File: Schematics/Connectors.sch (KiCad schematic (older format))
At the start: 106 parts, among them P601 CONN_02X05, P602 CONN_02X05, P603 CONN_02X05, P604 CONN_02X05, P605 CONN_02X05, P606 CONN_6X2, P607 CONN_02X05, P608 CONN_02X05, P609 CONN_02X20, P610 CONN_02X05, P611 CONN_02X05, P612 CONN_02X05, P613 CONN_02X05, P614 CONN_02X05, P615 CONN_02X05, P616 CONN_02X05

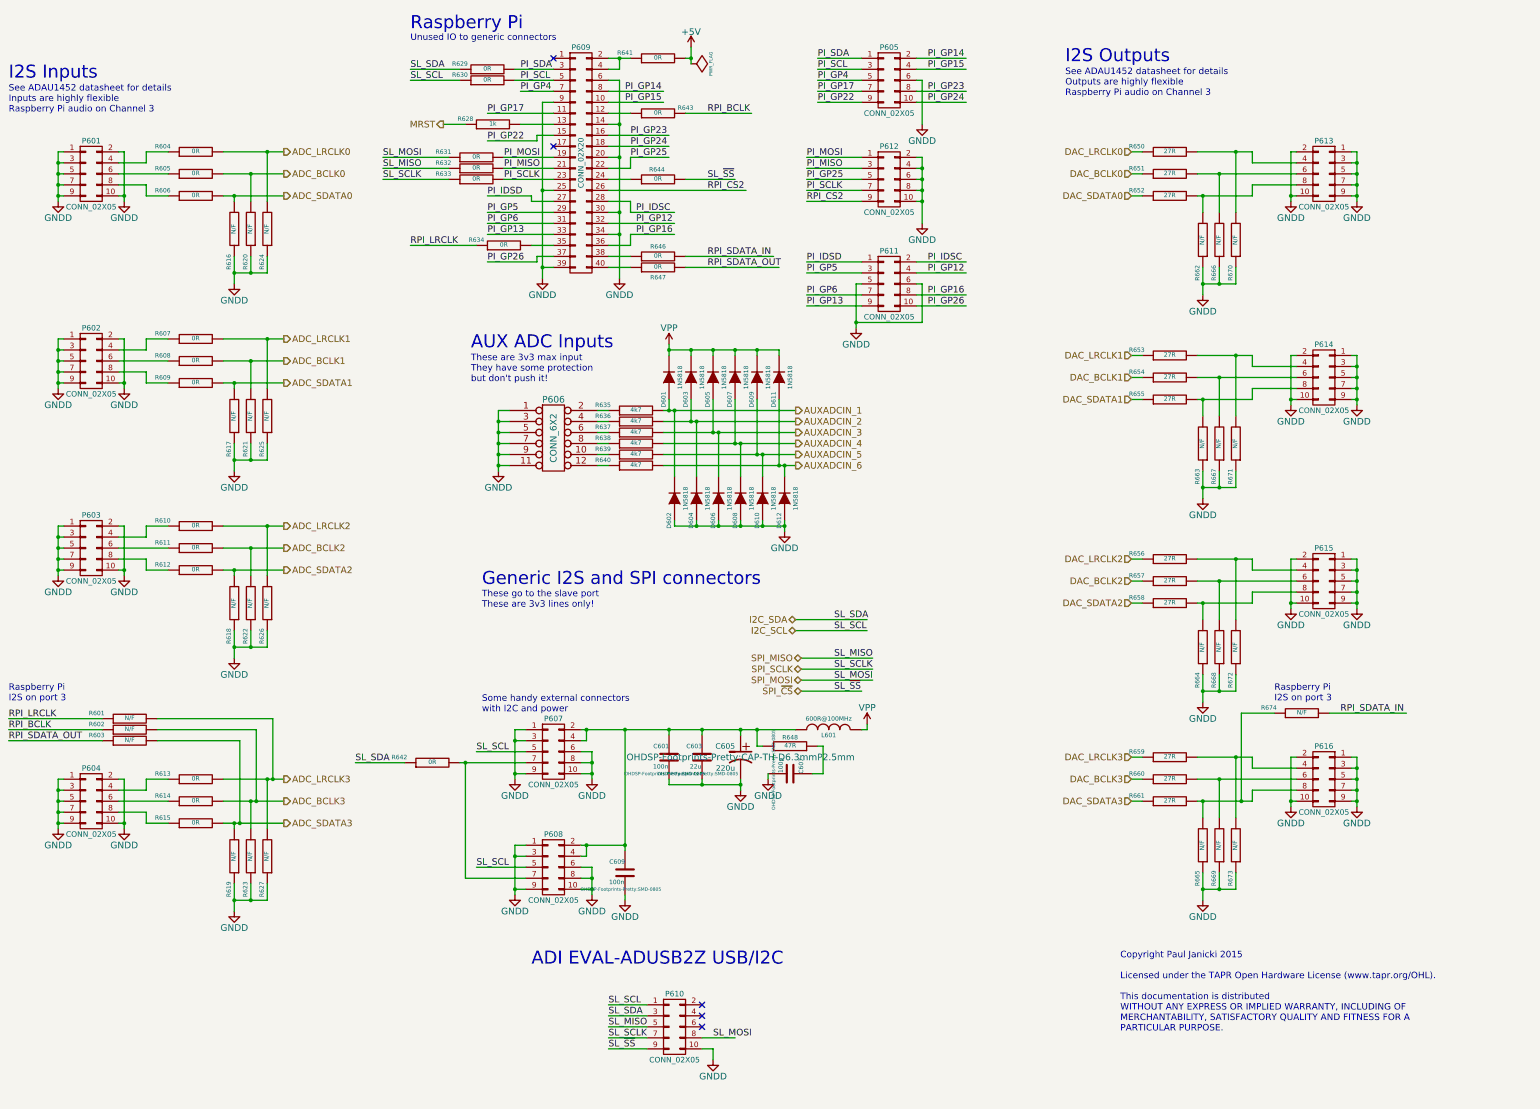
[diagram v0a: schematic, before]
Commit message: WIP
Removed Slave SPI as only really need I2C
Should free up some space on the board.
May look to change U.fl to SMA
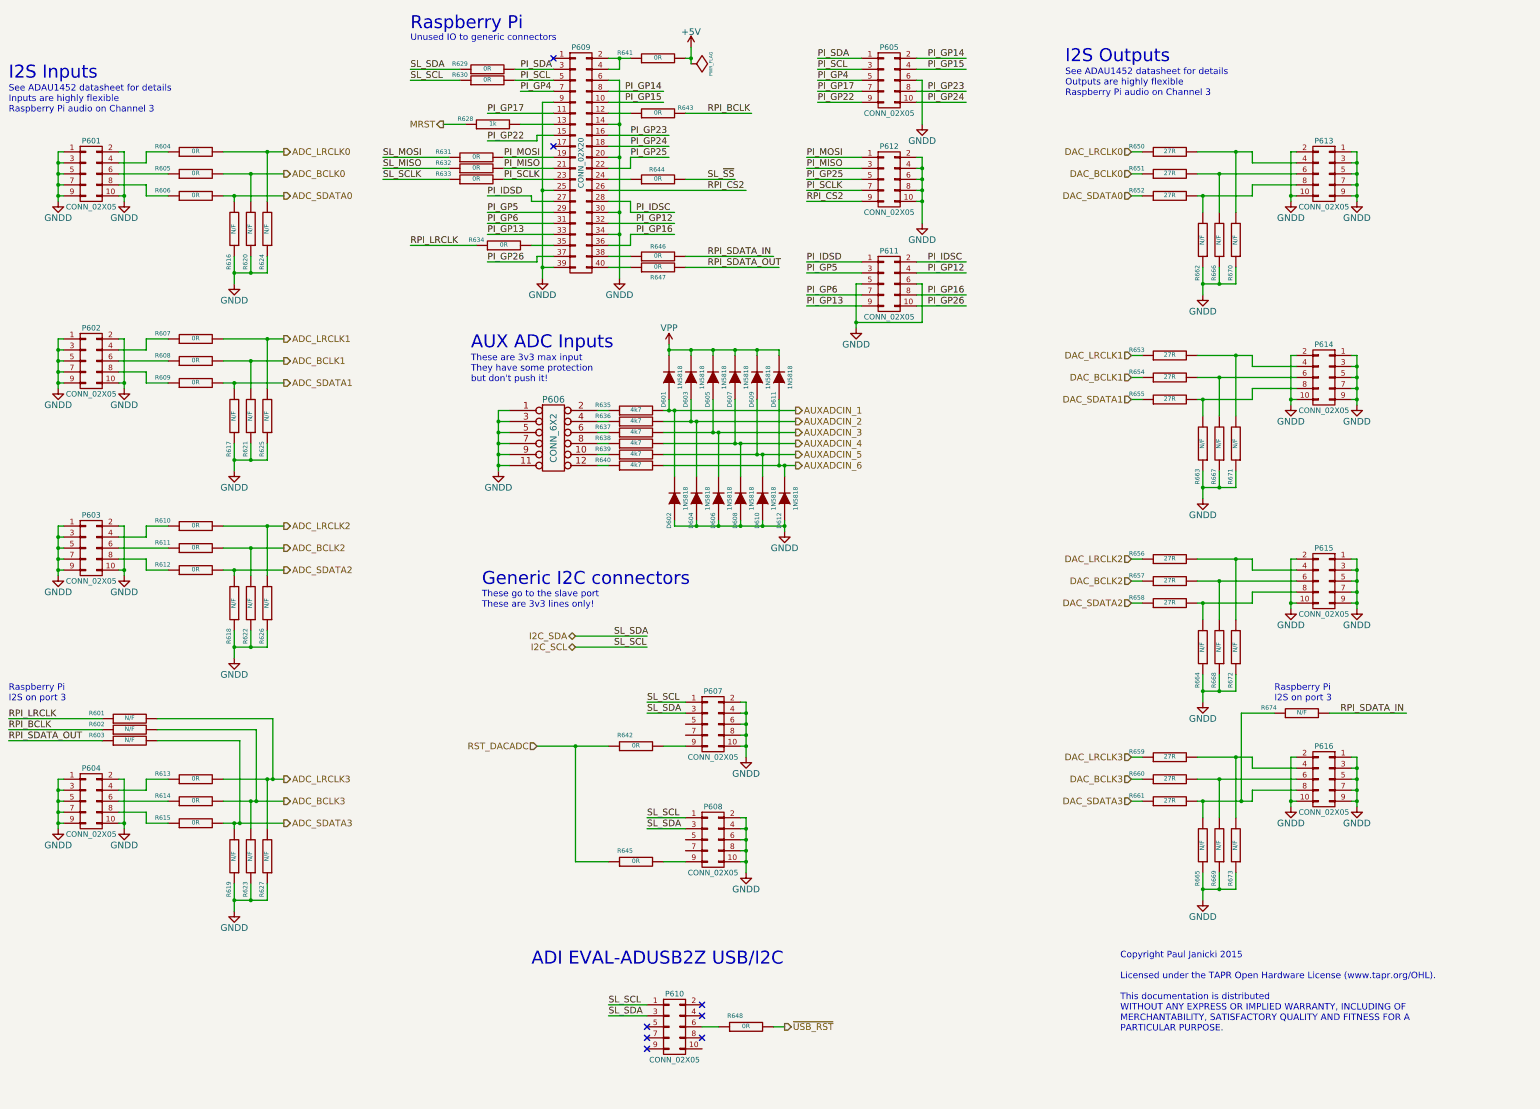
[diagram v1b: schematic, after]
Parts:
- removed C601, C609: 100n, OHDSP-Footprints-Pretty:SMD-0805, symbol C
- removed C603: 22u, OHDSP-Footprints-Pretty:SMD-0805, symbol C
- removed C605: 220u, OHDSP-Footprints-Pretty:CAP-TH-D6.3mmP2.5mm, symbol CP1
- removed C607: 100p, OHDSP-Footprints-Pretty:SMD-0805, symbol C
- removed L601: 600R@100MHz, OHDSP-Footprints-Pretty:SMD-0805, symbol INDUCTOR
- added R645: 0R, OHDSP-Footprints-Pretty:SMD-0805, symbol R
- R648: value 47R -> 0R
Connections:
- net labels added: RST_DACADC, ~USB_RST
- net labels removed: SPI_MISO, SPI_MOSI, SPI_SCLK, SPI_~CS
- wire segments 425 -> 393
- no-connect marks 5 -> 8
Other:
- note added: "Generic I2C connectors\n"
- note removed: "Generic I2S and SPI connectors\n"
- note removed: "Some handy external connectors\nwith I2C and power"
- moved on the sheet: P607, P608

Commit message: WIP
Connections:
- net labels added: PI_RST_OUT
- net labels removed: MRST
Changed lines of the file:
@@
 Copyright Paul Janicki 2015\n\nLicensed under the TAPR Open Hardware License (www.tapr.org/OHL).\n\nThis documentation is distributed\nWITHOUT ANY EXPRESS OR IMPLIED WARRANTY, INCLUDING OF\nMERCHANTABILITY, SATISFACTORY QUALITY AND FITNESS FOR A\nPARTICULAR PURPOSE.\n
 Text HLabel 5700 2300 0    60   Output ~ 0
-MRST
+PI_RST_OUT
 $Comp
 L CONN_02X05 P605

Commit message: WIP
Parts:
- P601, P602, P603, P604, P613, P614, P615, P616: footprint OHDSP-Footprints-Pretty:CONN_DIL_2X5 -> OHDSP-Footprints-Pretty:CONN_DIL_2X5_BOX
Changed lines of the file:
@@
 F 0 "P601" H 2500 3050 50  0000 C CNN
 F 1 "CONN_02X05" H 2500 2450 50  0000 C CNN
-F 2 "OHDSP-Footprints-Pretty:CONN_DIL_2X5" H 2500 1550 60  0001 C CNN
+F 2 "OHDSP-Footprints-Pretty:CONN_DIL_2X5_BOX" H 2500 1550 60  0001 C CNN
 F 3 "" H 2500 1550 60  0000 C CNN
 	1    2500 2750
@@
 F 0 "P602" H 2500 4750 50  0000 C CNN
 F 1 "CONN_02X05" H 2500 4150 50  0000 C CNN
-F 2 "OHDSP-Footprints-Pretty:CONN_DIL_2X5" H 2500 3250 60  0001 C CNN
+F 2 "OHDSP-Footprints-Pretty:CONN_DIL_2X5_BOX" H 2500 3250 60  0001 C CNN
 F 3 "" H 2500 3250 60  0000 C CNN
 	1    2500 4450
@@
 F 0 "P603" H 2500 6450 50  0000 C CNN
 F 1 "CONN_02X05" H 2500 5850 50  0000 C CNN
-F 2 "OHDSP-Footprints-Pretty:CONN_DIL_2X5" H 2500 4950 60  0001 C CNN
+F 2 "OHDSP-Footprints-Pretty:CONN_DIL_2X5_BOX" H 2500 4950 60  0001 C CNN
 F 3 "" H 2500 4950 60  0000 C CNN
 	1    2500 6150
@@
 F 0 "P604" H 2500 8750 50  0000 C CNN
 F 1 "CONN_02X05" H 2500 8150 50  0000 C CNN
-F 2 "OHDSP-Footprints-Pretty:CONN_DIL_2X5" H 2500 7250 60  0001 C CNN
+F 2 "OHDSP-Footprints-Pretty:CONN_DIL_2X5_BOX" H 2500 7250 60  0001 C CNN
 F 3 "" H 2500 7250 60  0000 C CNN
 	1    2500 8450
@@
 F 0 "P614" H 13700 4900 50  0000 C CNN
 F 1 "CONN_02X05" H 13700 4300 50  0000 C CNN
-F 2 "OHDSP-Footprints-Pretty:CONN_DIL_2X5" H 13700 3400 60  0001 C CNN
+F 2 "OHDSP-Footprints-Pretty:CONN_DIL_2X5_BOX" H 13700 3400 60  0001 C CNN
 F 3 "" H 13700 3400 60  0000 C CNN
 	1    13700 4600
@@
 F 0 "P615" H 13700 6750 50  0000 C CNN
 F 1 "CONN_02X05" H 13700 6150 50  0000 C CNN
-F 2 "OHDSP-Footprints-Pretty:CONN_DIL_2X5" H 13700 5250 60  0001 C CNN
+F 2 "OHDSP-Footprints-Pretty:CONN_DIL_2X5_BOX" H 13700 5250 60  0001 C CNN
 F 3 "" H 13700 5250 60  0000 C CNN
 	1    13700 6450
@@
 F 0 "P616" H 13700 8550 50  0000 C CNN
 F 1 "CONN_02X05" H 13700 7950 50  0000 C CNN
-F 2 "OHDSP-Footprints-Pretty:CONN_DIL_2X5" H 13700 7050 60  0001 C CNN
+F 2 "OHDSP-Footprints-Pretty:CONN_DIL_2X5_BOX" H 13700 7050 60  0001 C CNN
 F 3 "" H 13700 7050 60  0000 C CNN
 	1    13700 8250
@@
 F 0 "P613" H 13700 3050 50  0000 C CNN
 F 1 "CONN_02X05" H 13700 2450 50  0000 C CNN
-F 2 "OHDSP-Footprints-Pretty:CONN_DIL_2X5" H 13700 1550 60  0001 C CNN
+F 2 "OHDSP-Footprints-Pretty:CONN_DIL_2X5_BOX" H 13700 1550 60  0001 C CNN
 F 3 "" H 13700 1550 60  0000 C CNN
 	1    13700 2750
